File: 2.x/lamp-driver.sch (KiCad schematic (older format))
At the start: 67 parts, among them P4 CONN_16, P5 CONN_16, Q13 BC846, Q14 BC846, Q15 DMP2240UDM, Q16 DMN3190LDW-7, Q17 BC846, Q18 BC846, Q19 BC846, Q20 BC846, Q21 DMP2240UDM, Q22 DMN3190LDW-7, Q23 BC846, Q24 BC846

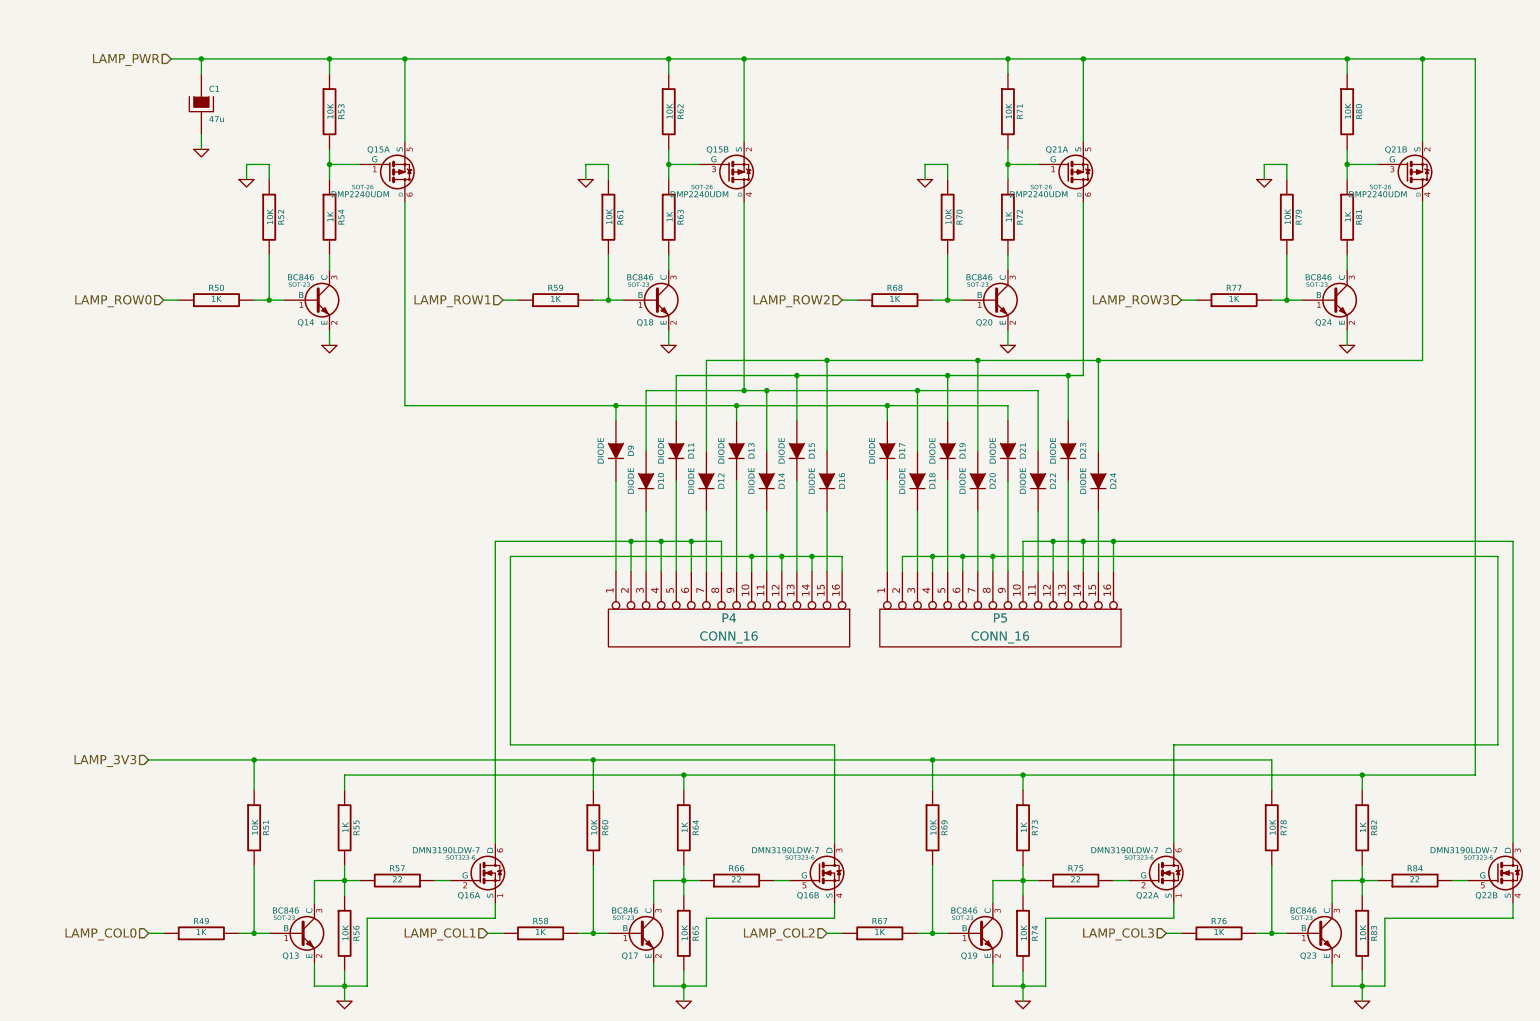
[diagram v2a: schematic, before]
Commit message: Cleaning up schematic Updating solenoid driver to use 12V for MOSFET gates instead of Vsol so we never exceed Vgs_max
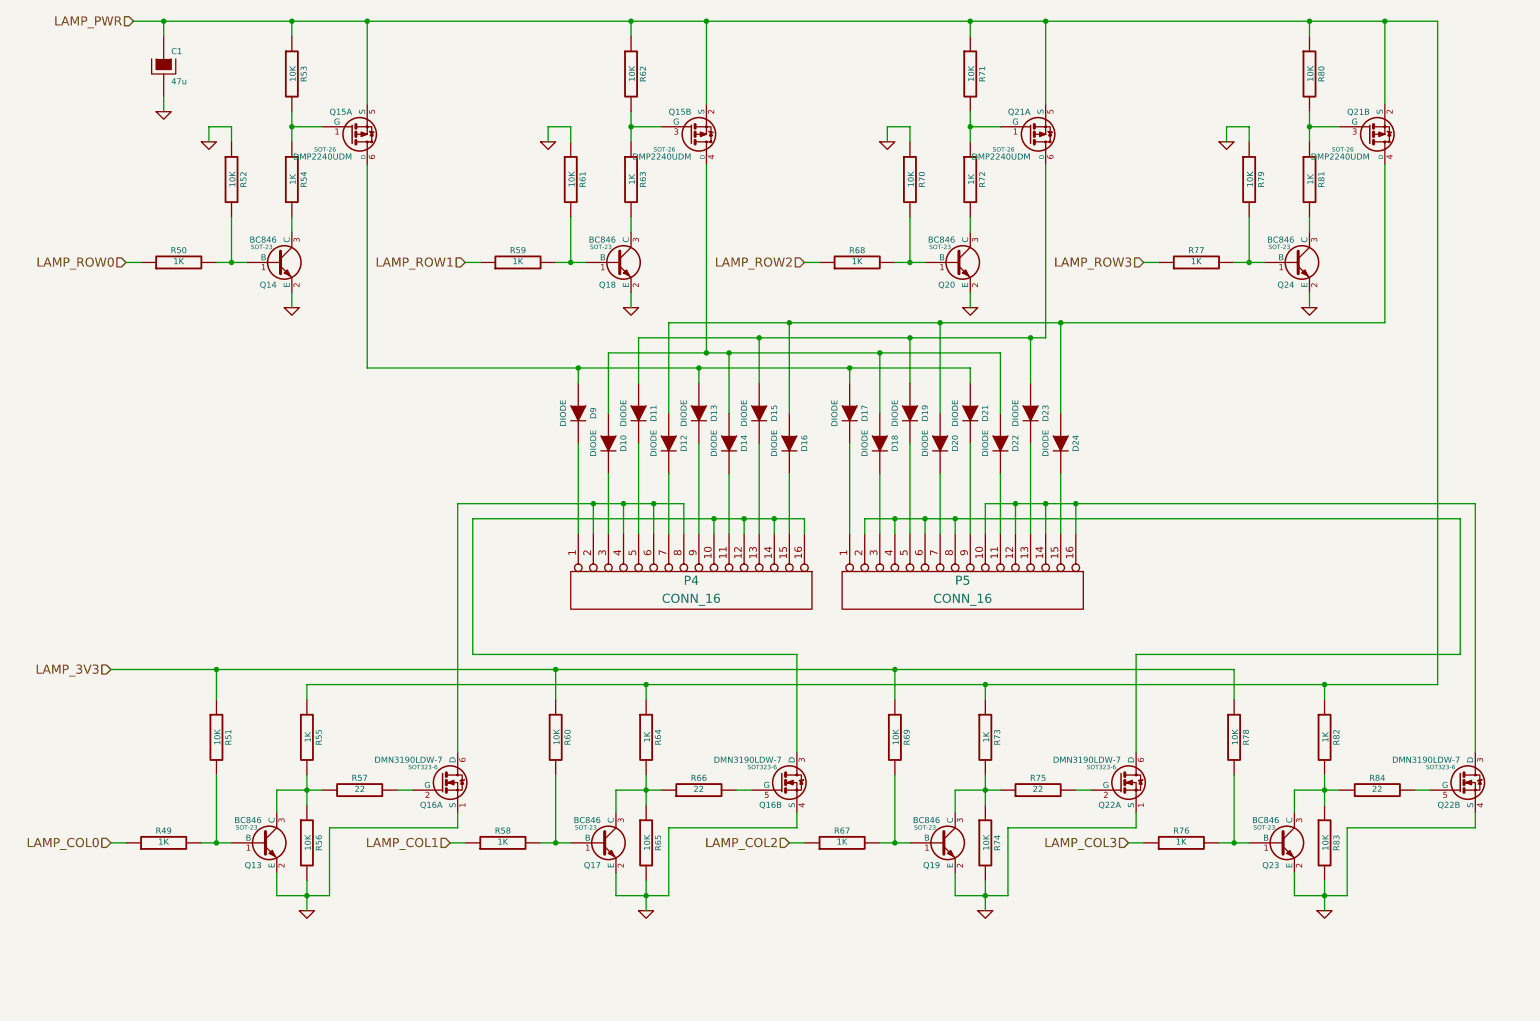
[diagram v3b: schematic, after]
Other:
- moved on the sheet: C1, D10, D11, D12, D13, D14, D15, D16, D17, D18, D19, D20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

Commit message: Started layout on 2.0
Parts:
- removed Q16, Q22: DMN3190LDW-7, SOT323-6, symbol DMN3190LDW-7
- added Q19, Q20: DMN6040SSD, Housings_SOIC:SOIC-8_3.9x4.9mm_Pitch1.27mm, symbol DMN6040SSD
- C1: footprint ~ -> Capacitors_SMD:c_elec_8x10
- D10: renamed from D11; value DIODE -> S1M; footprint ~ -> Diodes_SMD:Diode-SMA_Standard
- D11: renamed from D13; value DIODE -> S1M; footprint ~ -> Diodes_SMD:Diode-SMA_Standard
- D12: renamed from D15; value DIODE -> S1M; footprint ~ -> Diodes_SMD:Diode-SMA_Standard
- D13: renamed from D17; value DIODE -> S1M; footprint ~ -> Diodes_SMD:Diode-SMA_Standard
- D14: renamed from D19; value DIODE -> S1M; footprint ~ -> Diodes_SMD:Diode-SMA_Standard
- D15: renamed from D21; value DIODE -> S1M; footprint ~ -> Diodes_SMD:Diode-SMA_Standard
- D16: renamed from D23; value DIODE -> S1M; footprint ~ -> Diodes_SMD:Diode-SMA_Standard
- D17: renamed from D10; value DIODE -> S1M; footprint ~ -> Diodes_SMD:Diode-SMA_Standard
- D18: renamed from D12; value DIODE -> S1M; footprint ~ -> Diodes_SMD:Diode-SMA_Standard
- D19: renamed from D14; value DIODE -> S1M; footprint ~ -> Diodes_SMD:Diode-SMA_Standard
- D20: renamed from D16; value DIODE -> S1M; footprint ~ -> Diodes_SMD:Diode-SMA_Standard
- D21: renamed from D18; value DIODE -> S1M; footprint ~ -> Diodes_SMD:Diode-SMA_Standard
- D22: renamed from D20; value DIODE -> S1M; footprint ~ -> Diodes_SMD:Diode-SMA_Standard
- D23: renamed from D22; value DIODE -> S1M; footprint ~ -> Diodes_SMD:Diode-SMA_Standard
- D24, D9: value DIODE -> S1M; footprint ~ -> Diodes_SMD:Diode-SMA_Standard
- P4, P5: footprint (none) -> PinballParts:Socket_MOLEX-KK-RM2-54mm_Lock_16pin_straight
- Q13: renamed from Q15; footprint SOT-26 -> Housings_SOT-23_SOT-143_TSOT-6:SOT-23-6
- Q14: renamed from Q21; footprint SOT-26 -> Housings_SOT-23_SOT-143_TSOT-6:SOT-23-6
- Q15: renamed from Q14; footprint SOT-23 -> Housings_SOT-23_SOT-143_TSOT-6:SOT-23
- Q16: renamed from Q18; footprint SOT-23 -> Housings_SOT-23_SOT-143_TSOT-6:SOT-23
- Q17: renamed from Q20; footprint SOT-23 -> Housings_SOT-23_SOT-143_TSOT-6:SOT-23
- Q18: renamed from Q24; footprint SOT-23 -> Housings_SOT-23_SOT-143_TSOT-6:SOT-23
- Q21: renamed from Q13; footprint SOT-23 -> Housings_SOT-23_SOT-143_TSOT-6:SOT-23
- Q22: renamed from Q17; footprint SOT-23 -> Housings_SOT-23_SOT-143_TSOT-6:SOT-23
- Q23: renamed from Q19; footprint SOT-23 -> Housings_SOT-23_SOT-143_TSOT-6:SOT-23
- Q24: renamed from Q23; footprint SOT-23 -> Housings_SOT-23_SOT-143_TSOT-6:SOT-23
- R49: renamed from R53; footprint ~ -> Resistors_SMD:R_0603
- R50: renamed from R62; footprint ~ -> Resistors_SMD:R_0603
- R51: renamed from R71; footprint ~ -> Resistors_SMD:R_0603
- R52: renamed from R80; footprint ~ -> Resistors_SMD:R_0603
- R53: renamed from R52; footprint ~ -> Resistors_SMD:R_0603
- R54, R69, R75: footprint ~ -> Resistors_SMD:R_0603
- R55: renamed from R61; footprint ~ -> Resistors_SMD:R_0603
- R56: renamed from R63; footprint ~ -> Resistors_SMD:R_0603
- R57: renamed from R70; footprint ~ -> Resistors_SMD:R_0603
- R58: renamed from R72; footprint ~ -> Resistors_SMD:R_0603
- R59: renamed from R79; footprint ~ -> Resistors_SMD:R_0603
- R60: renamed from R81; footprint ~ -> Resistors_SMD:R_0603
- R61: renamed from R50; footprint ~ -> Resistors_SMD:R_0603
- R62: renamed from R59; footprint ~ -> Resistors_SMD:R_0603
- R63: renamed from R68; footprint ~ -> Resistors_SMD:R_0603
- R64: renamed from R77; footprint ~ -> Resistors_SMD:R_0603
- R65: renamed from R51; footprint ~ -> Resistors_SMD:R_0603
- R66: renamed from R55; footprint ~ -> Resistors_SMD:R_0603
- R67: renamed from R60; footprint ~ -> Resistors_SMD:R_0603
- R68: renamed from R64; footprint ~ -> Resistors_SMD:R_0603
- R70: renamed from R73; footprint ~ -> Resistors_SMD:R_0603
- R71: renamed from R78; footprint ~ -> Resistors_SMD:R_0603
- R72: renamed from R82; footprint ~ -> Resistors_SMD:R_0603
- R73: renamed from R57; footprint ~ -> Resistors_SMD:R_0603
- R74: renamed from R66; footprint ~ -> Resistors_SMD:R_0603
- R76: renamed from R84; footprint ~ -> Resistors_SMD:R_0603
- R77: renamed from R49; footprint ~ -> Resistors_SMD:R_0603
- R78: renamed from R56; footprint ~ -> Resistors_SMD:R_0603
- R79: renamed from R58; footprint ~ -> Resistors_SMD:R_0603
- R80: renamed from R65; footprint ~ -> Resistors_SMD:R_0603
- R81: renamed from R67; footprint ~ -> Resistors_SMD:R_0603
- R82: renamed from R74; footprint ~ -> Resistors_SMD:R_0603
- R83: renamed from R76; footprint ~ -> Resistors_SMD:R_0603
- R84: renamed from R83; footprint ~ -> Resistors_SMD:R_0603
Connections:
- net GND: now also Q19.1 (S), Q19.3 (1), Q20.1 (S), Q20.3 (1)
- net at P4.10 (P10), P4.12 (P12), P4.14 (P14)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: now also Q19.5 (D2), Q19.6 (D1)
- net at P4.2 (P2), P4.4 (P4), P4.6 (P6)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: now also Q19.7 (D2), Q19.8 (D1)
- net at P5.10 (P10), P5.12 (P12), P5.14 (P14)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: now also Q20.5 (D2), Q20.6 (D1)
- net at P5.2 (P2), P5.4 (P4), P5.6 (P6)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: now also Q20.7 (D2), Q20.8 (D1)
- net at R76.2: now also Q20.4 (G)
- net at R75.2: now also Q20.2 (G)
- net at R74.2: now also Q19.4 (G)
- net at R73.1: now also Q19.2 (G)
- net LAMP_PWR renamed LAMP_12V

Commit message: Committing latest files. This includes the KiCAD 4.0.0rc1 migration as well as the updates to Base Board 2.1.
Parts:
- removed D10, D11, D12, D13, D14, D15, D16, D17, D18, D19, D20, D21, D22, D23, D24, D9: S1M, Diodes_SMD:Diode-SMA_Standard, symbol DIODE
- added D10, D11, D12, D13, D14, D15, D16, D17, D18, D19, D20, D21, D22, D23, D24, D9: S1M, Diodes_SMD:SMA_Standard, symbol D
- C1: symbol CP -> CP-RESCUE-base-module-hardware-v2
- R49, R50, R51, R52, R53, R54, R55, R56, R57, R58, R59, R60, R61, R62, R63, R64, R65, R66, R67, R68, R69, R70, R71, R72, R73, R74, R75, R76, R77, R78, R79, R80, R81, R82, R83, R84: symbol R -> R-RESCUE-base-module-hardware-v2
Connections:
- net at Q13.6 (D): now also D11.2 (A), D13.2 (A), D15.2 (A), D9.2 (A)
- net at P4.1 (P1): now also D9.1 (K)
- net at Q13.4 (D): now also D17.2 (A), D19.2 (A), D21.2 (A), D23.2 (A)
- net at P4.3 (P3): now also D17.1 (K)
- net at Q14.6 (D): now also D10.2 (A), D12.2 (A), D14.2 (A), D16.2 (A)
- net at P4.5 (P5): now also D10.1 (K)
- net at Q14.4 (D): now also D18.2 (A), D20.2 (A), D22.2 (A), D24.2 (A)
- net at P4.7 (P7): now also D18.1 (K)
- net at P4.9 (P9): now also D11.1 (K)
- net at P4.11 (P11): now also D19.1 (K)
- net at P4.13 (P13): now also D12.1 (K)
- net at P4.15 (P15): now also D20.1 (K)
- net at P5.1 (P1): now also D13.1 (K)
- net at P5.3 (P3): now also D21.1 (K)
- net at P5.5 (P5): now also D14.1 (K)
- net at P5.7 (P7): now also D22.1 (K)
- net at P5.9 (P9): now also D15.1 (K)
- net at P5.11 (P11): now also D23.1 (K)
- net at P5.13 (P13): now also D16.1 (K)
- net at P5.15 (P15): now also D24.1 (K)
